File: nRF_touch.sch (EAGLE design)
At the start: 92 parts, among them IC1 MCP73831/OT, Q1 BSS138BKW, T1 BSS84, T2 BC847, T3 BC847, T4 BC847, U1 ADP160, U2 AT42QT1040, Y1 32.768kHz, Y2 32MHz-3.2X2.5

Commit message: Errors corrected #1
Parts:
- removed U3: (no value), adafruit:GPS_FGPMMOPA6H
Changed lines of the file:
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@@
 <part name="R15" library="SparkFun-Resistors" deviceset="4.7KOHM" device="-0603-1/10W-1%" value="10k"/>
 <part name="GND1" library="SparkFun-PowerSymbols" deviceset="GND" device=""/>
-<part name="U3" library="adafruit" deviceset="GPS_FGPMMOPA6H" device=""/>
 <part name="J1" library="SparkFun-Connectors" deviceset="CONN_02" device=""/>
 <part name="J4" library="SparkFun-Connectors" deviceset="CONN_02" device=""/>
@@
 <instance part="GND16" gate="1" x="2.54" y="81.28" rot="R90"/>
 <instance part="R12" gate="G$1" x="-22.86" y="81.28" rot="R180"/>
-<instance part="U3" gate="G$1" x="58.42" y="71.12"/>
 <instance part="J1" gate="G$1" x="-124.46" y="58.42" rot="R90"/>
 <instance part="J4" gate="G$1" x="-111.76" y="58.42" rot="R90"/>
@@
 </segment>
 </net>
-<net name="NEO_DIN" class="1">
+<net name="NEO_DIN" class="0">
 <segment>
 <pinref part="Q1" gate="A" pin="D"/>

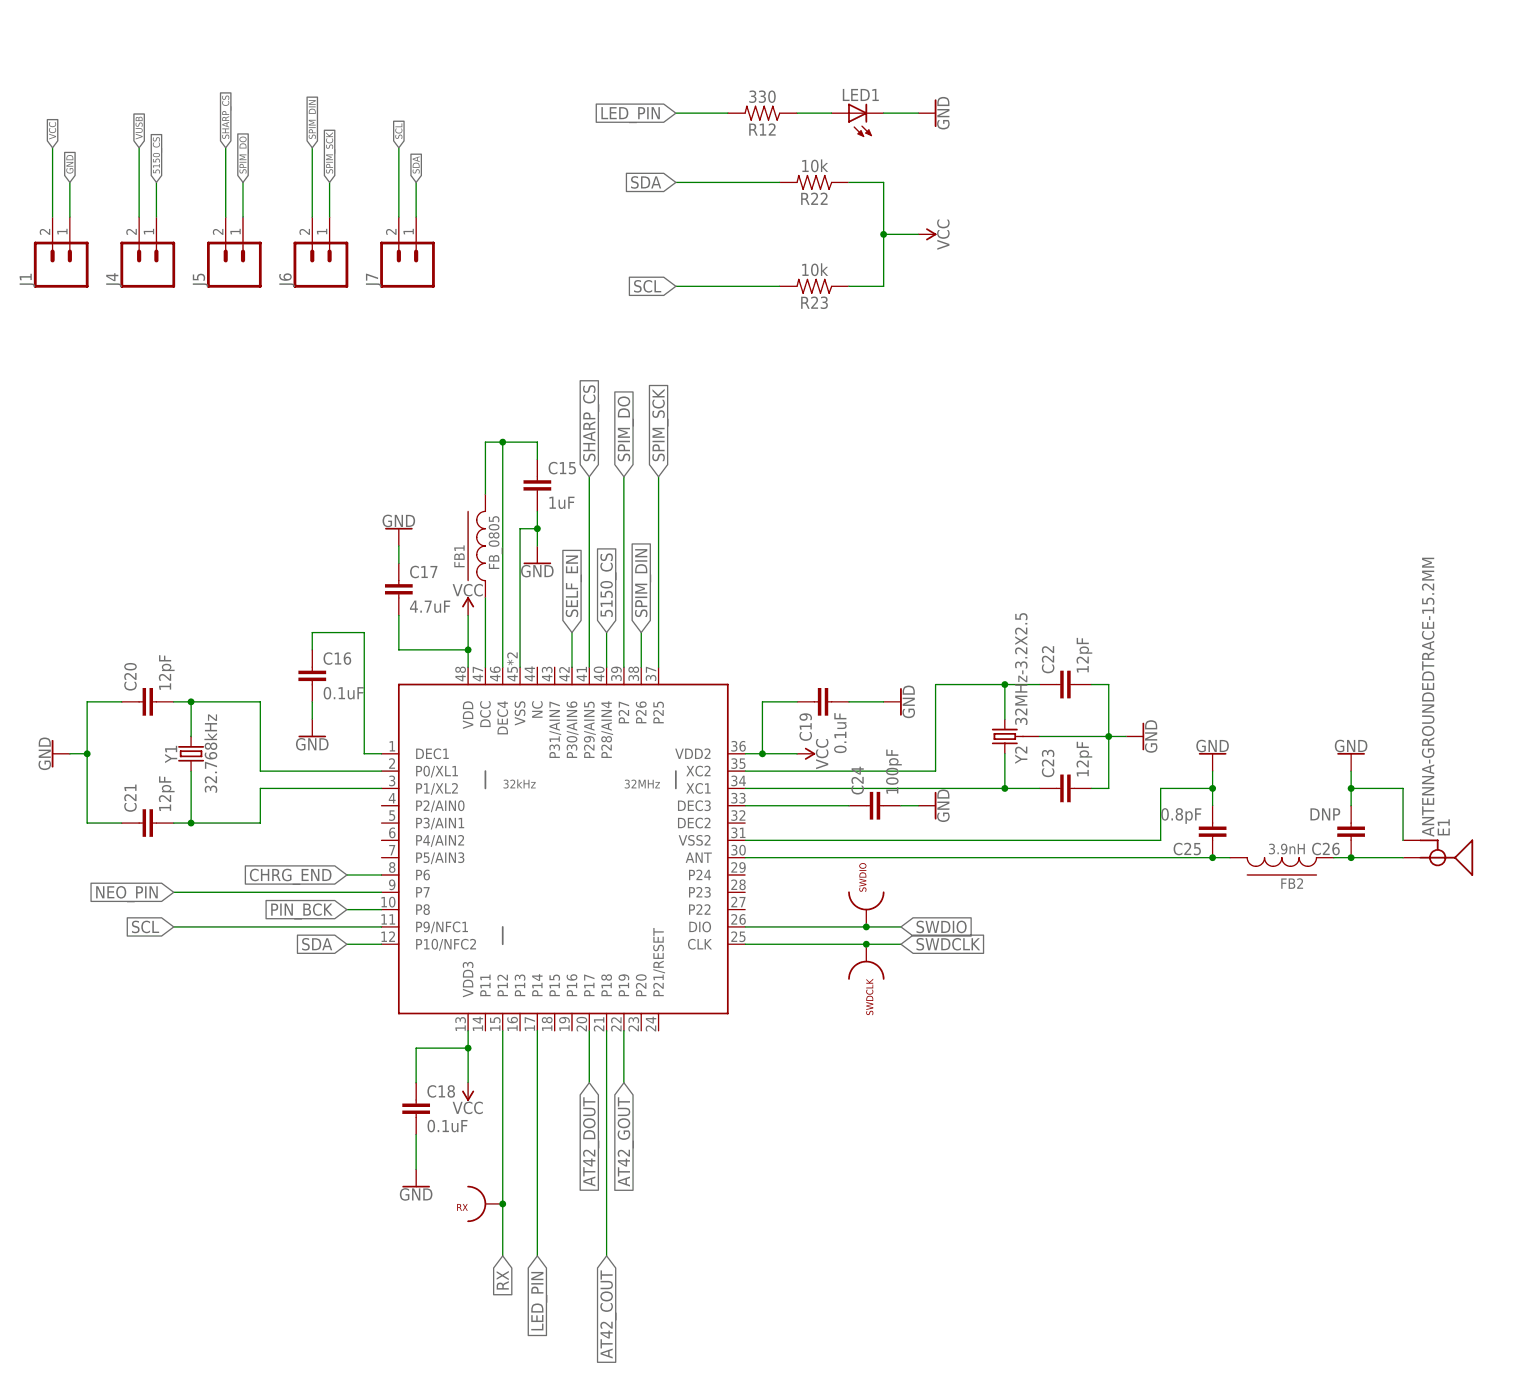
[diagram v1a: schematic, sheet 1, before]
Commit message: -Same dimensions for top and bottom -more pads exposed -different power distribution
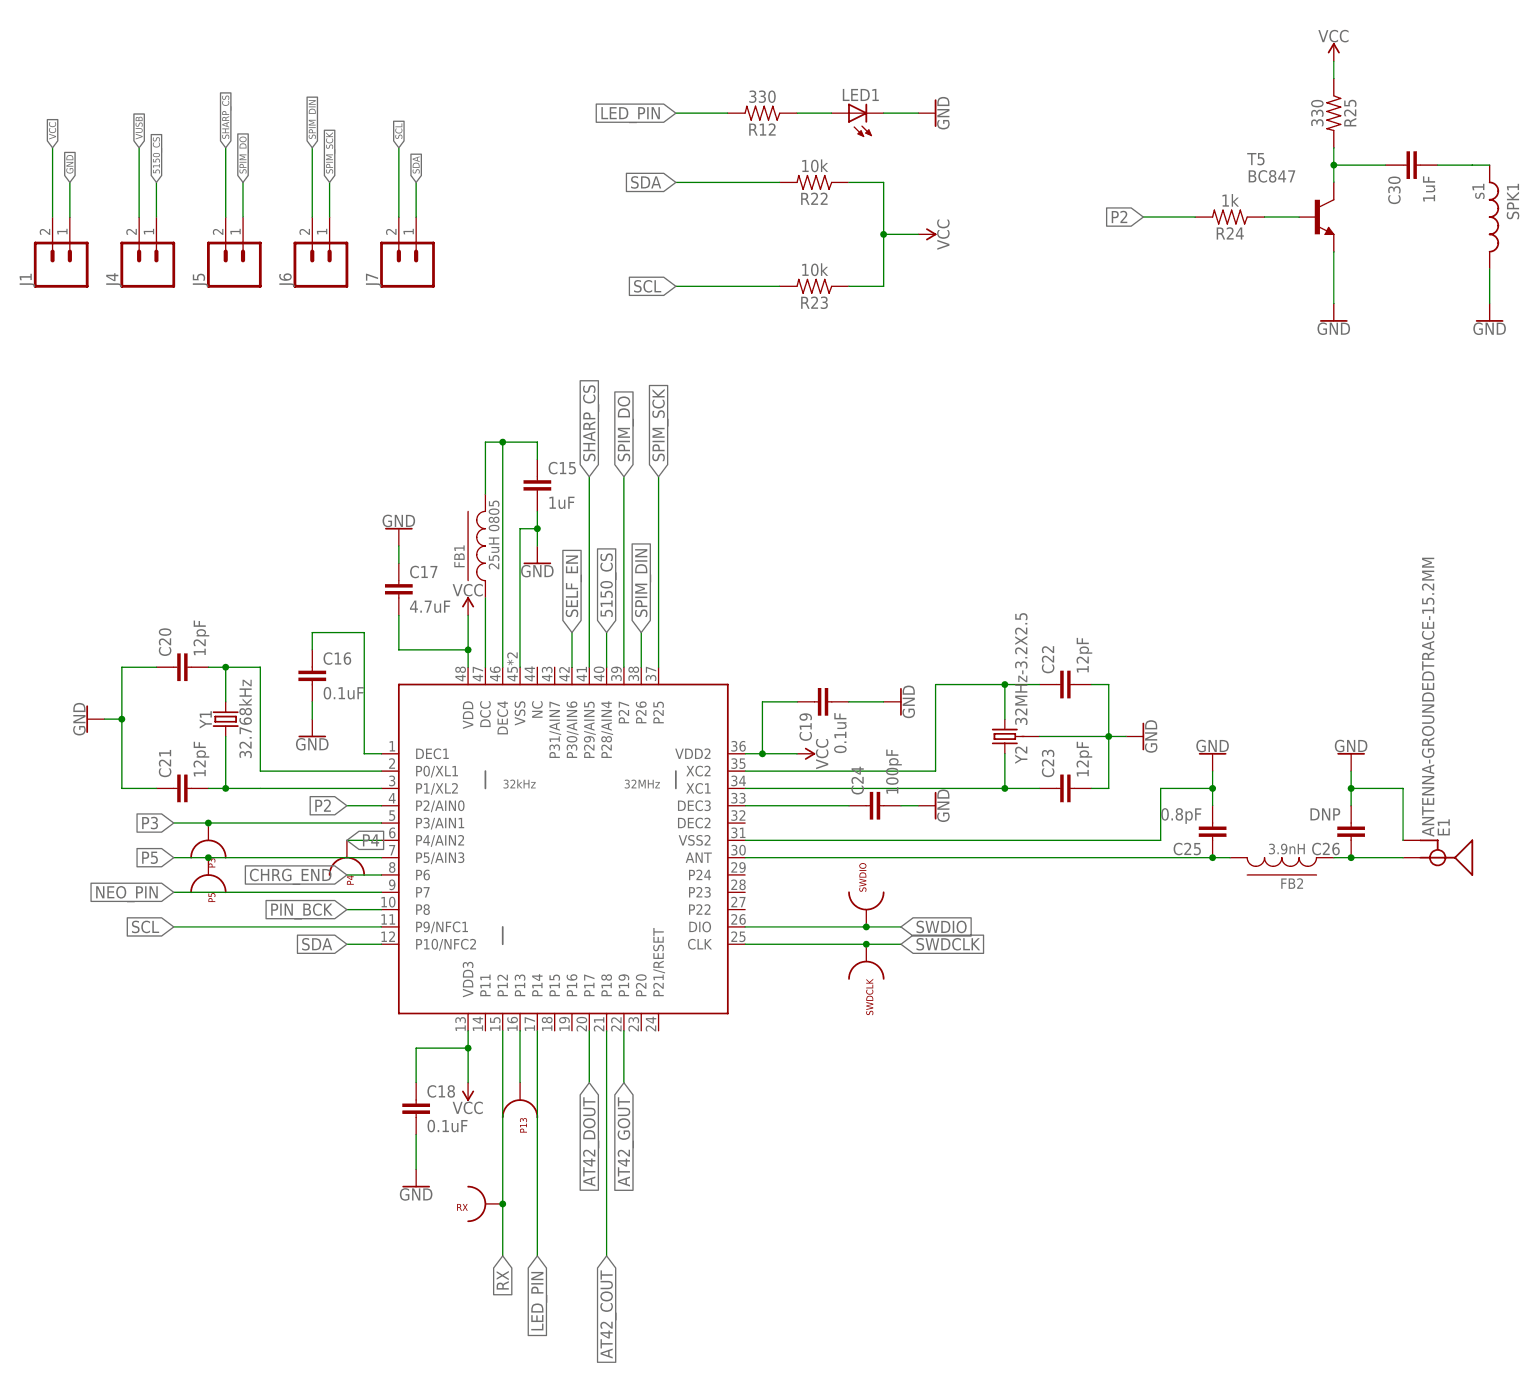
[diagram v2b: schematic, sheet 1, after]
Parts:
- added C30: 1uF, SparkFun-Capacitors:4.7UF0603
- added D1: BAT54C, nxp_60:BAT754C
- added P13, P4, P5: TESTPOINT_22, test_points:TESTPOINT_22
- added P3: p3, test_points:TESTPOINT_22
- added R24: 1k, SparkFun-Resistors:4.7KOHM-0603-1/10W-1%
- added R25: 330, SparkFun-Resistors:4.7KOHM-0603-1/10W-1%
- added SPK1: s1, Strutz Electronic Industries:MDMK2020T4R7MM
- added T5: BC847, nxp_60:BC847
- FB1: value FB_0805 -> 25uH 0805
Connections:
- new net LDO_VIN: D1.K1K2, U1.VIN
- new net N$10: C30.1, R25.2, T5.C
- new net N$29: C30.2, SPK1.1
- new net N$30: R24.1, T5.B
- new net P13: P13.P$1, U$6.P13
- new net P2: R24.2, U$6.P2/AIN0
- new net P3: P3.P$1, U$6.P3/AIN1
- new net P4: P4.P$1, U$6.P4/AIN2
- new net P5: P5.P$1, U$6.P5/AIN3
- net GND: now also SPK1.2, T5.E
- net VBAT: now also D1.A1; no longer U1.VIN
- net VCC: now also R25.1
- net VUSB: now also D1.A2
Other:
- moved on the sheet: C20, C21, Y1

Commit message: Routing done
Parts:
- removed D1: BAT54C, nxp_60:BAT754C
- removed J1, J4, J5, J6, J7: (no value), SparkFun-Connectors:CONN_02
- removed P3: p3, test_points:TESTPOINT_22
- removed P4: TESTPOINT_22, test_points:TESTPOINT_22
- removed R10: 10k, SparkFun-Resistors:4.7KOHM-0603-1/10W-1%
- removed R20: 47k, SparkFun-Resistors:4.7KOHM-0603-1/10W-1%
- removed R9: 100k, SparkFun-Resistors:4.7KOHM-0603-1/10W-1%
- removed T2: BC847, nxp_60:BC847
- added CONN2: 503480-1200, MOLEX12:503480-1200
- C9: value 0.1uF -> 4.7uF
- R19: value 0.010 -> 0.1
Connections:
- net N$15 renamed DEC3
- removed net LDO_VIN: D1.K1K2, U1.VIN
- removed net N$1: R9.2, T2.B
- removed net P3: P3.P$1, U$6.P3/AIN1
- removed net TRANS: D3.K1, T2.C
- new net AT42_EN: D3.K2, U2.OUT2
- new net STC_EN: D3.K1, U$3.IO
- net 5150_CS: now also CONN2.P$10; no longer J4.1
- net AT42_COUT: now also CONN2.P$1; no longer D3.K2
- net GND: now also CONN2.P$6; no longer J1.1, R10.2, R20.2, T2.E
- net P4: now also CONN2.P$3; no longer P4.P$1
- net SCL: now also CONN2.P$4; no longer J7.2
- net SDA: now also CONN2.P$5; no longer J7.1
- net SELF_EN: now also U2.SNS2; no longer R10.1, R9.1
- net SHARP_CS: now also CONN2.P$7; no longer J5.2
- net SPIM_DIN: now also CONN2.P$2; no longer J6.2
- net SPIM_DO: now also CONN2.P$8; no longer J5.1
- net SPIM_SCK: now also CONN2.P$9; no longer J6.1
- net SW_AT: no longer L1.VDD, R14.2
- net SW_POWER: now also L1.VDD, R14.2, U1.VIN; no longer C3.1, R2.2, R20.1, U$3.VCC
- net VBAT: now also C3.1, R2.2, U$3.VCC; no longer D1.A1
- net VCC: now also CONN2.P$11; no longer J1.2
- net VUSB: now also CONN2.P$12; no longer D1.A2, J4.2
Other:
- moved on the sheet: D2
